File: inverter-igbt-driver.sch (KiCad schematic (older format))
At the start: 10 parts, among them J1 Conn_01x06, J2 Conn_01x06, U9 IGBT_HALF_BRIDGE

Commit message: Completed layout with one connector.
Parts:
- removed J1, J2: Conn_01x06, Pin_Headers:Pin_Header_Straight_1x06_Pitch1.00mm, symbol Conn_01x06
- added J1: Conn_01x09, Pin_Headers:Pin_Header_Straight_1x09_Pitch2.54mm, symbol Conn_01x09
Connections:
- wire segments 54 -> 58
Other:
- moved on the sheet: R10, R4, R6, R7, R8, R9
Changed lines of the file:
@@
 Comment4 ""
 $EndDescr
-$Comp
-L Conn_01x06 J1
-U 1 1 5ACC5671
-P 3250 2250
-F 0 "J1" H 3250 2550 50  0000 C CNN
-F 1 "Conn_01x06" H 3250 1850 50  0000 C CNN
-F 2 "Pin_Headers:Pin_Header_Straight_1x06_Pitch1.00mm" H 3250 2250 50  0001 C CNN
-F 3 "" H 3250 2250 50  0001 C CNN
-	1    3250 2250
-	1    0    0    -1
-$EndComp
 Text Label 2850 2050 0    60   ~ 0
 GND
@@
 Text Label 2850 2350 0    60   ~ 0
 VIN_H
-Text Notes 2200 1750 0    60   ~ 0
+Text Notes 1950 1750 0    60   ~ 0
 Incoming header for IO and Power Supply
 $Comp
 L R R4
 U 1 1 5ACCB4A7
-P 2650 2750
-F 0 "R4" V 2730 2750 50  0000 C CNN
-F 1 "1k" V 2650 2750 50  0000 C CNN
-F 2 "Resistors_SMD:R_0402" V 2580 2750 50  0001 C CNN
-F 3 "" H 2650 2750 50  0001 C CNN
-	1    2650 2750
+P 2550 3100
+F 0 "R4" V 2630 3100 50  0000 C CNN
+F 1 "1k" V 2550 3100 50  0000 C CNN
+F 2 "Resistors_SMD:R_0402" V 2480 3100 50  0001 C CNN
+F 3 "" H 2550 3100 50  0001 C CNN
+	1    2550 3100
 	1    0    0    -1
 $EndComp
@@
 L R R6
 U 1 1 5ACCE827
-P 2350 2200
-F 0 "R6" V 2430 2200 50  0000 C CNN
-F 1 "1k" V 2350 2200 50  0000 C CNN
-F 2 "Resistors_SMD:R_0402" V 2280 2200 50  0001 C CNN
-F 3 "" H 2350 2200 50  0001 C CNN
-	1    2350 2200
+P 1650 2200
+F 0 "R6" V 1730 2200 50  0000 C CNN
+F 1 "1k" V 1650 2200 50  0000 C CNN
+F 2 "Resistors_SMD:R_0402" V 1580 2200 50  0001 C CNN
+F 3 "" H 1650 2200 50  0001 C CNN
+	1    1650 2200
 	1    0    0    -1
 $EndComp
@@
 L R R7
 U 1 1 5ACCE8BE
-P 2550 2200
-F 0 "R7" V 2630 2200 50  0000 C CNN
-F 1 "1k" V 2550 2200 50  0000 C CNN
-F 2 "Resistors_SMD:R_0402" V 2480 2200 50  0001 C CNN
-F 3 "" H 2550 2200 50  0001 C CNN
-	1    2550 2200
+P 1850 2200
+F 0 "R7" V 1930 2200 50  0000 C CNN
+F 1 "1k" V 1850 2200 50  0000 C CNN
+F 2 "Resistors_SMD:R_0402" V 1780 2200 50  0001 C CNN
+F 3 "" H 1850 2200 50  0001 C CNN
+	1    1850 2200
 	1    0    0    -1
 $EndComp
@@
 L GND #PWR01
 U 1 1 5ACCE97E
-P 2650 2950
-F 0 "#PWR01" H 2650 2700 50  0001 C CNN
-F 1 "GND" H 2650 2800 50  0000 C CNN
-F 2 "" H 2650 2950 50  0001 C CNN
-F 3 "" H 2650 2950 50  0001 C CNN
-	1    2650 2950
-	1    0    0    -1
-$EndComp
-Text Notes 1200 2500 0    60   ~ 0
+P 2650 3350
+F 0 "#PWR01" H 2650 3100 50  0001 C CNN
+F 1 "GND" H 2650 3200 50  0000 C CNN
+F 2 "" H 2650 3350 50  0001 C CNN
+F 3 "" H 2650 3350 50  0001 C CNN
+	1    2650 3350
+	1    0    0    -1
+$EndComp
+Text Notes 700  1650 0    60   ~ 0
 Pull-Up/Down Resistors
 $Comp
@@
 $EndComp
 Wire Wire Line
-	2550 2450 3050 2450
-Wire Wire Line
-	2550 2450 2550 2350
-Wire Wire Line
-	2350 2550 3050 2550
-Wire Wire Line
-	2350 2550 2350 2350
-Wire Wire Line
-	2650 2350 3050 2350
-Wire Wire Line
-	2650 2350 2650 2600
-Wire Wire Line
-	2650 2900 2650 2950
+	1850 2450 3050 2450
+Wire Wire Line
+	1850 2450 1850 2350
+Wire Wire Line
+	1650 2550 3050 2550
+Wire Wire Line
+	1650 2550 1650 2350
+Wire Wire Line
+	2550 2350 3050 2350
+Wire Wire Line
+	2550 2350 2550 2950
 $Comp
 L +5V #PWR02
 U 1 1 5ACD9AA7
-P 2450 1950
-F 0 "#PWR02" H 2450 1800 50  0001 C CNN
-F 1 "+5V" H 2450 2090 50  0000 C CNN
-F 2 "" H 2450 1950 50  0001 C CNN
-F 3 "" H 2450 1950 50  0001 C CNN
-	1    2450 1950
-	1    0    0    -1
-$EndComp
-Wire Wire Line
-	2350 2050 2350 2000
-Wire Wire Line
-	2350 2000 2550 2000
-Wire Wire Line
-	2550 2000 2550 2050
-Wire Wire Line
-	2450 1950 2450 2000
-Connection ~ 2450 2000
+P 1550 1950
+F 0 "#PWR02" H 1550 1800 50  0001 C CNN
+F 1 "+5V" H 1550 2090 50  0000 C CNN
+F 2 "" H 1550 1950 50  0001 C CNN
+F 3 "" H 1550 1950 50  0001 C CNN
+	1    1550 1950
+	1    0    0    -1
+$EndComp
+Wire Wire Line
+	1650 2000 1650 2050
+Wire Wire Line
+	1250 2000 1450 2000
+Wire Wire Line
+	1450 2000 1550 2000
+Wire Wire Line
+	1550 2000 1650 2000
+Wire Wire Line
+	1650 2000 1850 2000
+Wire Wire Line
+	1850 2000 1850 2050
+Wire Wire Line
+	1550 1950 1550 2000
+Connection ~ 1550 2000
 $Sheet
 S 7050 1950 1000 800
@@
 Wire Wire Line
 	7050 3250 6850 3250
-$Comp
-L Conn_01x06 J2
-U 1 1 5ADA8100
-P 3250 3800
-F 0 "J2" H 3250 4100 50  0000 C CNN
-F 1 "Conn_01x06" H 3250 3400 50  0000 C CNN
-F 2 "Pin_Headers:Pin_Header_Straight_1x06_Pitch1.00mm" H 3250 3800 50  0001 C CNN
-F 3 "" H 3250 3800 50  0001 C CNN
-	1    3250 3800
-	1    0    0    -1
-$EndComp
-Text Label 2850 3600 0    60   ~ 0
-GND
-Text Label 2850 3700 0    60   ~ 0
-+5V
-Text Label 2850 3800 0    60   ~ 0
-+24V
-Text Label 2850 4000 0    60   ~ 0
+Text Label 2850 2750 0    60   ~ 0
 FAULT_L
-Text Label 2850 4100 0    60   ~ 0
+Text Label 2850 2850 0    60   ~ 0
 RESET_L
-Text Label 2850 3900 0    60   ~ 0
+Text Label 2850 2650 0    60   ~ 0
 VIN_L
-Text Notes 2200 3300 0    60   ~ 0
-Incoming header for IO and Power Supply
 $Comp
 L R R10
 U 1 1 5ADA810E
-P 2650 4300
-F 0 "R10" V 2730 4300 50  0000 C CNN
-F 1 "1k" V 2650 4300 50  0000 C CNN
-F 2 "Resistors_SMD:R_0402" V 2580 4300 50  0001 C CNN
-F 3 "" H 2650 4300 50  0001 C CNN
-	1    2650 4300
-	1    0    0    -1
-$EndComp
-Wire Wire Line
-	3050 3700 2850 3700
-Wire Wire Line
-	3050 3800 2850 3800
+P 2750 3100
+F 0 "R10" V 2830 3100 50  0000 C CNN
+F 1 "1k" V 2750 3100 50  0000 C CNN
+F 2 "Resistors_SMD:R_0402" V 2680 3100 50  0001 C CNN
+F 3 "" H 2750 3100 50  0001 C CNN
+	1    2750 3100
+	1    0    0    -1
+$EndComp
 $Comp
 L R R8
 U 1 1 5ADA8118
-P 2350 3750
-F 0 "R8" V 2430 3750 50  0000 C CNN
-F 1 "1k" V 2350 3750 50  0000 C CNN
-F 2 "Resistors_SMD:R_0402" V 2280 3750 50  0001 C CNN
-F 3 "" H 2350 3750 50  0001 C CNN
-	1    2350 3750
+P 1250 2200
+F 0 "R8" V 1330 2200 50  0000 C CNN
+F 1 "1k" V 1250 2200 50  0000 C CNN
+F 2 "Resistors_SMD:R_0402" V 1180 2200 50  0001 C CNN
+F 3 "" H 1250 2200 50  0001 C CNN
+	1    1250 2200
 	1    0    0    -1
 $EndComp
@@
 L R R9
 U 1 1 5ADA811F
-P 2550 3750
-F 0 "R9" V 2630 3750 50  0000 C CNN
-F 1 "1k" V 2550 3750 50  0000 C CNN
-F 2 "Resistors_SMD:R_0402" V 2480 3750 50  0001 C CNN
-F 3 "" H 2550 3750 50  0001 C CNN
-	1    2550 3750
-	1    0    0    -1
-$EndComp
-$Comp
-L GND #PWR03
-U 1 1 5ADA8126
-P 2650 4500
-F 0 "#PWR03" H 2650 4250 50  0001 C CNN
-F 1 "GND" H 2650 4350 50  0000 C CNN
-F 2 "" H 2650 4500 50  0001 C CNN
-F 3 "" H 2650 4500 50  0001 C CNN
-	1    2650 4500
-	1    0    0    -1
-$EndComp
-Text Notes 1200 4050 0    60   ~ 0
-Pull-Up/Down Resistors
-Wire Wire Line
-	2550 4000 3050 4000
-Wire Wire Line
-	2550 4000 2550 3900
-Wire Wire Line
-	2350 4100 3050 4100
-Wire Wire Line
-	2350 4100 2350 3900
-Wire Wire Line
-	2650 3900 3050 3900
-Wire Wire Line
-	2650 3900 2650 4150
-Wire Wire Line
-	2650 4450 2650 4500
-$Comp
-L +5V #PWR04
-U 1 1 5ADA813B
-P 2450 3500
-F 0 "#PWR04" H 2450 3350 50  0001 C CNN
-F 1 "+5V" H 2450 3640 50  0000 C CNN
-F 2 "" H 2450 3500 50  0001 C CNN
-F 3 "" H 2450 3500 50  0001 C CNN
-	1    2450 3500
-	1    0    0    -1
-$EndComp
-Wire Wire Line
-	2350 3600 2350 3550
-Wire Wire Line
-	2350 3550 2550 3550
-Wire Wire Line
-	2550 3550 2550 3600
-Wire Wire Line
-	2450 3500 2450 3550
-Connection ~ 2450 3550
+P 1450 2200
+F 0 "R9" V 1530 2200 50  0000 C CNN
+F 1 "1k" V 1450 2200 50  0000 C CNN
+F 2 "Resistors_SMD:R_0402" V 1380 2200 50  0001 C CNN
+F 3 "" H 1450 2200 50  0001 C CNN
+	1    1450 2200
+	1    0    0    -1
+$EndComp
 $Comp
 L IGBT_HALF_BRIDGE U9
@@
 $EndComp
 Wire Wire Line
-	8600 2450 8600 3150
+	8600 2450 8600 2800
+Wire Wire Line
+	8600 2800 8600 3150
 Wire Wire Line
 	8900 2800 8600 2800
@@
 $EndSheet
 Wire Wire Line
-	5550 2450 7050 2450
-Wire Wire Line
-	7000 2550 5550 2550
+	5550 2450 6450 2450
+Wire Wire Line
+	6450 2450 7050 2450
+Wire Wire Line
+	5550 2550 6400 2550
+Wire Wire Line
+	6400 2550 7050 2550
 Wire Wire Line
 	7050 3450 6450 3450
@@
 	6400 3550 6400 2550
 Connection ~ 6400 2550
-Wire Wire Line
-	3050 3600 2850 3600
+$Comp
+L Conn_01x09 J1
+U 1 1 5ADBF612
+P 3250 2450
+F 0 "J1" H 3250 2950 50  0000 C CNN
+F 1 "Conn_01x09" H 3250 1950 50  0000 C CNN
+F 2 "Pin_Headers:Pin_Header_Straight_1x09_Pitch2.54mm" H 3250 2450 50  0001 C CNN
+F 3 "" H 3250 2450 50  0001 C CNN
+	1    3250 2450
+	1    0    0    -1
+$EndComp
+Wire Wire Line
+	1250 2850 3050 2850
+Wire Wire Line
+	1250 2850 1250 2350
+Wire Wire Line
+	1450 2750 3050 2750
+Wire Wire Line
+	1450 2750 1450 2350
+Wire Wire Line
+	1450 2050 1450 2000
+Connection ~ 1650 2000
+Wire Wire Line
+	1250 2050 1250 2000
+Connection ~ 1450 2000
+Wire Wire Line
+	2750 2950 2750 2650
+Wire Wire Line
+	2750 2650 3050 2650
+Wire Wire Line
+	2550 3250 2550 3300
+Wire Wire Line
+	2550 3300 2650 3300
+Wire Wire Line
+	2650 3300 2750 3300
+Wire Wire Line
+	2750 3300 2750 3250
+Wire Wire Line
+	2650 3350 2650 3300
+Connection ~ 2650 3300
 $EndSCHEMATC

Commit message: Wire adjustments
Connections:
- wire segments 58 -> 51
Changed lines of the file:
@@
 	1650 2000 1650 2050
 Wire Wire Line
-	1250 2000 1450 2000
-Wire Wire Line
-	1450 2000 1550 2000
-Wire Wire Line
-	1550 2000 1650 2000
-Wire Wire Line
-	1650 2000 1850 2000
+	1250 2000 1850 2000
 Wire Wire Line
 	1850 2000 1850 2050
@@
 $EndComp
 Wire Wire Line
-	8600 2450 8600 2800
-Wire Wire Line
-	8600 2800 8600 3150
+	8600 2450 8600 3150
 Wire Wire Line
 	8900 2800 8600 2800
@@
 $EndSheet
 Wire Wire Line
-	5550 2450 6450 2450
-Wire Wire Line
-	6450 2450 7050 2450
-Wire Wire Line
-	5550 2550 6400 2550
-Wire Wire Line
-	6400 2550 7050 2550
+	5550 2450 7050 2450
+Wire Wire Line
+	5550 2550 7050 2550
 Wire Wire Line
 	7050 3450 6450 3450
@@
 	2550 3250 2550 3300
 Wire Wire Line
-	2550 3300 2650 3300
-Wire Wire Line
-	2650 3300 2750 3300
+	2550 3300 2750 3300
 Wire Wire Line
 	2750 3300 2750 3250

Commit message: Adds NTC to connector.
Completes 555 rewire.

Rewires IGBT signals to layout more simply.
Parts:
- removed J1: Conn_01x09, Pin_Headers:Pin_Header_Straight_1x09_Pitch2.54mm, symbol Conn_01x09
- added J1: CONTROL, Pin_Headers:Pin_Header_Straight_1x11_Pitch2.54mm, symbol Conn_01x11
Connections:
- net labels added: NTC+, NTC-
- wire segments 51 -> 55
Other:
- moved on the sheet: R10, R4, R6, R7, R8, R9
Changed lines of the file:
@@
 Text Label 2850 2250 0    60   ~ 0
 +24V
+Text Label 2850 2350 0    60   ~ 0
+FAULT_H
 Text Label 2850 2450 0    60   ~ 0
-FAULT_H
+RESET_H
 Text Label 2850 2550 0    60   ~ 0
-RESET_H
-Text Label 2850 2350 0    60   ~ 0
 VIN_H
 Text Notes 1950 1750 0    60   ~ 0
@@
 L R R4
 U 1 1 5ACCB4A7
-P 2550 3100
-F 0 "R4" V 2630 3100 50  0000 C CNN
-F 1 "1k" V 2550 3100 50  0000 C CNN
-F 2 "Resistors_SMD:R_0402" V 2480 3100 50  0001 C CNN
-F 3 "" H 2550 3100 50  0001 C CNN
-	1    2550 3100
+P 2400 3100
+F 0 "R4" V 2480 3100 50  0000 C CNN
+F 1 "1k" V 2400 3100 50  0000 C CNN
+F 2 "Resistors_SMD:R_0402" V 2330 3100 50  0001 C CNN
+F 3 "" H 2400 3100 50  0001 C CNN
+	1    2400 3100
 	1    0    0    -1
 $EndComp
@@
 L R R6
 U 1 1 5ACCE827
-P 1650 2200
-F 0 "R6" V 1730 2200 50  0000 C CNN
-F 1 "1k" V 1650 2200 50  0000 C CNN
-F 2 "Resistors_SMD:R_0402" V 1580 2200 50  0001 C CNN
-F 3 "" H 1650 2200 50  0001 C CNN
-	1    1650 2200
+P 1650 2100
+F 0 "R6" V 1730 2100 50  0000 C CNN
+F 1 "1k" V 1650 2100 50  0000 C CNN
+F 2 "Resistors_SMD:R_0402" V 1580 2100 50  0001 C CNN
+F 3 "" H 1650 2100 50  0001 C CNN
+	1    1650 2100
 	1    0    0    -1
 $EndComp
@@
 L R R7
 U 1 1 5ACCE8BE
-P 1850 2200
-F 0 "R7" V 1930 2200 50  0000 C CNN
-F 1 "1k" V 1850 2200 50  0000 C CNN
-F 2 "Resistors_SMD:R_0402" V 1780 2200 50  0001 C CNN
-F 3 "" H 1850 2200 50  0001 C CNN
-	1    1850 2200
+P 1850 2100
+F 0 "R7" V 1930 2100 50  0000 C CNN
+F 1 "1k" V 1850 2100 50  0000 C CNN
+F 2 "Resistors_SMD:R_0402" V 1780 2100 50  0001 C CNN
+F 3 "" H 1850 2100 50  0001 C CNN
+	1    1850 2100
 	1    0    0    -1
 $EndComp
@@
 L GND #PWR01
 U 1 1 5ACCE97E
-P 2650 3350
-F 0 "#PWR01" H 2650 3100 50  0001 C CNN
-F 1 "GND" H 2650 3200 50  0000 C CNN
-F 2 "" H 2650 3350 50  0001 C CNN
-F 3 "" H 2650 3350 50  0001 C CNN
-	1    2650 3350
+P 2500 3350
+F 0 "#PWR01" H 2500 3100 50  0001 C CNN
+F 1 "GND" H 2500 3200 50  0000 C CNN
+F 2 "" H 2500 3350 50  0001 C CNN
+F 3 "" H 2500 3350 50  0001 C CNN
+	1    2500 3350
 	1    0    0    -1
 $EndComp
@@
 	1    0    0    -1
 $EndComp
-Wire Wire Line
-	1850 2450 3050 2450
-Wire Wire Line
-	1850 2450 1850 2350
-Wire Wire Line
-	1650 2550 3050 2550
-Wire Wire Line
-	1650 2550 1650 2350
-Wire Wire Line
-	2550 2350 3050 2350
-Wire Wire Line
-	2550 2350 2550 2950
 $Comp
 L +5V #PWR02
 U 1 1 5ACD9AA7
-P 1550 1950
-F 0 "#PWR02" H 1550 1800 50  0001 C CNN
-F 1 "+5V" H 1550 2090 50  0000 C CNN
-F 2 "" H 1550 1950 50  0001 C CNN
-F 3 "" H 1550 1950 50  0001 C CNN
-	1    1550 1950
-	1    0    0    -1
-$EndComp
-Wire Wire Line
-	1650 2000 1650 2050
-Wire Wire Line
-	1250 2000 1850 2000
-Wire Wire Line
-	1850 2000 1850 2050
-Wire Wire Line
-	1550 1950 1550 2000
-Connection ~ 1550 2000
+P 1550 1850
+F 0 "#PWR02" H 1550 1700 50  0001 C CNN
+F 1 "+5V" H 1550 1990 50  0000 C CNN
+F 2 "" H 1550 1850 50  0001 C CNN
+F 3 "" H 1550 1850 50  0001 C CNN
+	1    1550 1850
+	1    0    0    -1
+$EndComp
+Wire Wire Line
+	1650 1900 1650 1950
+Wire Wire Line
+	1250 1900 1850 1900
+Wire Wire Line
+	1850 1900 1850 1950
+Wire Wire Line
+	1550 1850 1550 1900
+Connection ~ 1550 1900
 $Sheet
 S 7050 1950 1000 800
@@
 Wire Wire Line
 	7050 3250 6850 3250
+Text Label 2850 2650 0    60   ~ 0
+FAULT_L
 Text Label 2850 2750 0    60   ~ 0
-FAULT_L
+RESET_L
 Text Label 2850 2850 0    60   ~ 0
-RESET_L
-Text Label 2850 2650 0    60   ~ 0
 VIN_L
 $Comp
 L R R10
 U 1 1 5ADA810E
-P 2750 3100
-F 0 "R10" V 2830 3100 50  0000 C CNN
-F 1 "1k" V 2750 3100 50  0000 C CNN
-F 2 "Resistors_SMD:R_0402" V 2680 3100 50  0001 C CNN
-F 3 "" H 2750 3100 50  0001 C CNN
-	1    2750 3100
+P 2600 3100
+F 0 "R10" V 2680 3100 50  0000 C CNN
+F 1 "1k" V 2600 3100 50  0000 C CNN
+F 2 "Resistors_SMD:R_0402" V 2530 3100 50  0001 C CNN
+F 3 "" H 2600 3100 50  0001 C CNN
+	1    2600 3100
 	1    0    0    -1
 $EndComp
@@
 L R R8
 U 1 1 5ADA8118
-P 1250 2200
-F 0 "R8" V 1330 2200 50  0000 C CNN
-F 1 "1k" V 1250 2200 50  0000 C CNN
-F 2 "Resistors_SMD:R_0402" V 1180 2200 50  0001 C CNN
-F 3 "" H 1250 2200 50  0001 C CNN
-	1    1250 2200
+P 1250 2100
+F 0 "R8" V 1330 2100 50  0000 C CNN
+F 1 "1k" V 1250 2100 50  0000 C CNN
+F 2 "Resistors_SMD:R_0402" V 1180 2100 50  0001 C CNN
+F 3 "" H 1250 2100 50  0001 C CNN
+	1    1250 2100
 	1    0    0    -1
 $EndComp
@@
 L R R9
 U 1 1 5ADA811F
-P 1450 2200
-F 0 "R9" V 1530 2200 50  0000 C CNN
-F 1 "1k" V 1450 2200 50  0000 C CNN
-F 2 "Resistors_SMD:R_0402" V 1380 2200 50  0001 C CNN
-F 3 "" H 1450 2200 50  0001 C CNN
-	1    1450 2200
+P 1450 2100
+F 0 "R9" V 1530 2100 50  0000 C CNN
+F 1 "1k" V 1450 2100 50  0000 C CNN
+F 2 "Resistors_SMD:R_0402" V 1380 2100 50  0001 C CNN
+F 3 "" H 1450 2100 50  0001 C CNN
+	1    1450 2100
 	1    0    0    -1
 $EndComp
@@
 	6400 3550 6400 2550
 Connection ~ 6400 2550
-$Comp
-L Conn_01x09 J1
-U 1 1 5ADBF612
-P 3250 2450
-F 0 "J1" H 3250 2950 50  0000 C CNN
-F 1 "Conn_01x09" H 3250 1950 50  0000 C CNN
-F 2 "Pin_Headers:Pin_Header_Straight_1x09_Pitch2.54mm" H 3250 2450 50  0001 C CNN
-F 3 "" H 3250 2450 50  0001 C CNN
-	1    3250 2450
-	1    0    0    -1
-$EndComp
-Wire Wire Line
-	1250 2850 3050 2850
-Wire Wire Line
-	1250 2850 1250 2350
-Wire Wire Line
-	1450 2750 3050 2750
-Wire Wire Line
-	1450 2750 1450 2350
-Wire Wire Line
-	1450 2050 1450 2000
-Connection ~ 1650 2000
-Wire Wire Line
-	1250 2050 1250 2000
-Connection ~ 1450 2000
-Wire Wire Line
-	2750 2950 2750 2650
-Wire Wire Line
-	2750 2650 3050 2650
-Wire Wire Line
-	2550 3250 2550 3300
-Wire Wire Line
-	2550 3300 2750 3300
-Wire Wire Line
-	2750 3300 2750 3250
-Wire Wire Line
-	2650 3350 2650 3300
-Connection ~ 2650 3300
+Wire Wire Line
+	1450 1950 1450 1900
+Connection ~ 1650 1900
+Wire Wire Line
+	1250 1950 1250 1900
+Connection ~ 1450 1900
+Wire Wire Line
+	2400 3250 2400 3300
+Wire Wire Line
+	2400 3300 2600 3300
+Wire Wire Line
+	2600 3300 2600 3250
+Wire Wire Line
+	2500 3350 2500 3300
+Connection ~ 2500 3300
+$Comp
+L Conn_01x11 J1
+U 1 1 5AF4D114
+P 3250 2550
+F 0 "J1" H 3250 3150 50  0000 C CNN
+F 1 "CONTROL" H 3250 1950 50  0000 C CNN
+F 2 "Pin_Headers:Pin_Header_Straight_1x11_Pitch2.54mm" H 3250 2550 50  0001 C CNN
+F 3 "" H 3250 2550 50  0001 C CNN
+	1    3250 2550
+	1    0    0    -1
+$EndComp
+Text Label 10450 2550 0    60   ~ 0
+NTC+
+Text Label 10450 3050 0    60   ~ 0
+NTC-
+Wire Wire Line
+	10450 2550 10300 2550
+Wire Wire Line
+	10450 3050 10300 3050
+Text Label 2850 2950 0    60   ~ 0
+NTC+
+Text Label 2850 3050 0    60   ~ 0
+NTC-
+Wire Wire Line
+	2850 2950 3050 2950
+Wire Wire Line
+	3050 3050 2850 3050
+Wire Wire Line
+	1450 2650 3050 2650
+Wire Wire Line
+	1450 2650 1450 2250
+Wire Wire Line
+	1250 2750 3050 2750
+Wire Wire Line
+	1250 2750 1250 2250
+Wire Wire Line
+	2600 2850 3050 2850
+Wire Wire Line
+	2600 2950 2600 2850
+Wire Wire Line
+	1850 2350 3050 2350
+Wire Wire Line
+	1850 2350 1850 2250
+Wire Wire Line
+	1650 2450 3050 2450
+Wire Wire Line
+	1650 2450 1650 2250
+Wire Wire Line
+	2400 2550 3050 2550
+Wire Wire Line
+	2400 2550 2400 2950
 $EndSCHEMATC

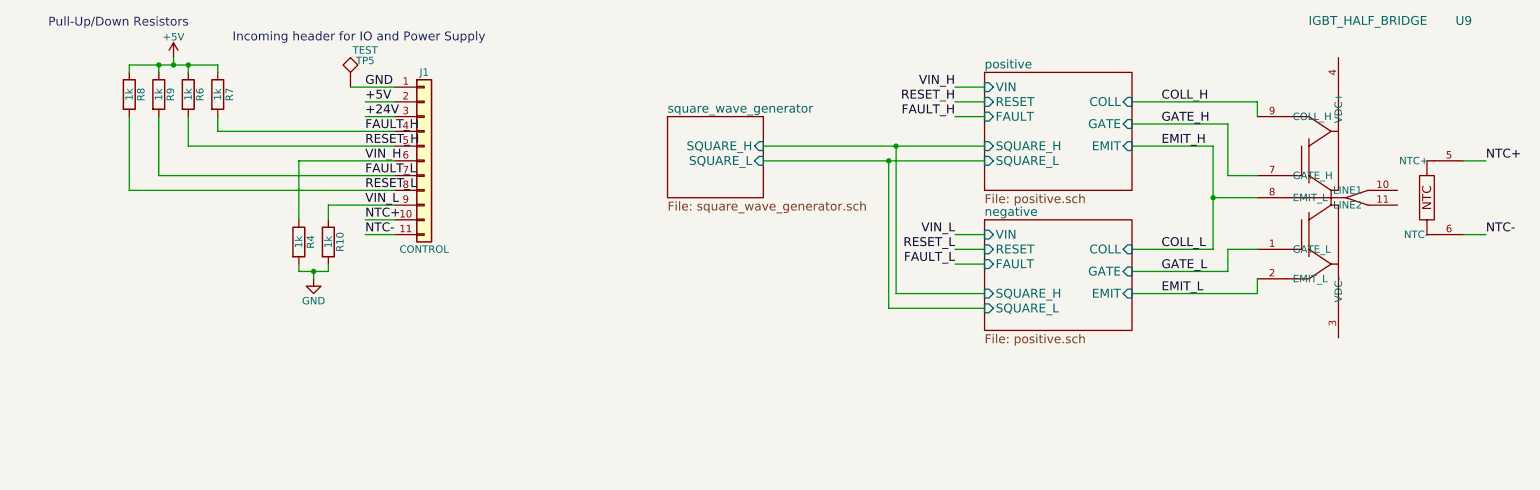
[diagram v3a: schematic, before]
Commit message: Cleaning up layout of main connector.
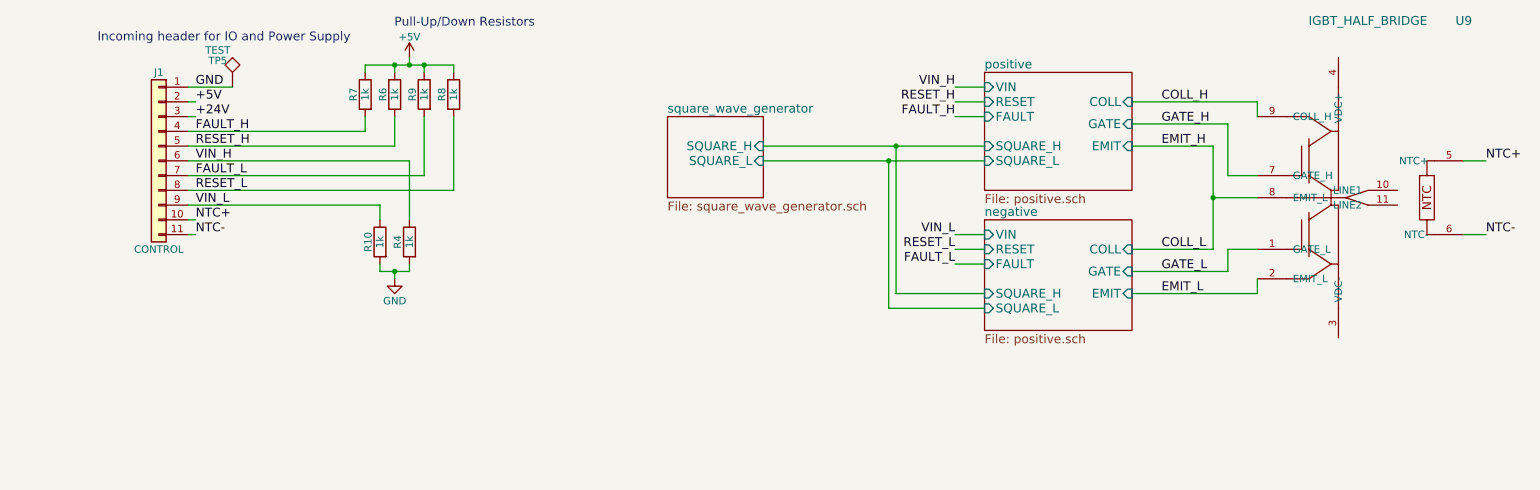
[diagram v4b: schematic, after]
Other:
- moved on the sheet: J1, R10, R4, R6, R7, R8, R9, TP5

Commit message: Adding d-flop to achieve 50% duty cycle
555 timer config cannot guarantee 50% duty cycle, but a frequency divider can.
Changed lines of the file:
@@
 	3050 1900 3050 1950
 Wire Wire Line
-	3450 1900 3250 1900
-Wire Wire Line
-	3250 1900 3150 1900
-Wire Wire Line
-	3150 1900 3050 1900
-Wire Wire Line
-	3050 1900 2850 1900
+	2850 1900 3450 1900
 Wire Wire Line
 	2850 1900 2850 1950
@@
 $EndComp
 Wire Wire Line
-	8600 2450 8600 2800
-Wire Wire Line
-	8600 2800 8600 3150
+	8600 2450 8600 3150
 Wire Wire Line
 	8900 2800 8600 2800
@@
 $EndSheet
 Wire Wire Line
-	5550 2450 6450 2450
+	5550 2450 7050 2450
 Wire Wire Line
-	6450 2450 7050 2450
-Wire Wire Line
-	5550 2550 6400 2550
-Wire Wire Line
-	6400 2550 7050 2550
+	5550 2550 7050 2550
 Wire Wire Line
 	7050 3450 6450 3450
@@
 Connection ~ 3050 1900
 Wire Wire Line
-	3450 1950 3450 1900
+	3450 1900 3450 1950
 Connection ~ 3250 1900
 Wire Wire Line
-	3150 3250 3150 3300
+	3150 3300 3150 3250
 Wire Wire Line
-	3150 3300 3050 3300
-Wire Wire Line
-	3050 3300 2950 3300
+	2950 3300 3150 3300
 Wire Wire Line
 	2950 3300 2950 3250
